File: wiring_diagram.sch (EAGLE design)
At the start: 9 parts, among them X1 22-23-2021, X2 22-23-2021, X3 22-23-2021, X4 22-23-2021, X5 22-23-2021, X6 22-23-2021, X7 22-23-2021, X8 22-23-2021, X9 22-23-2021

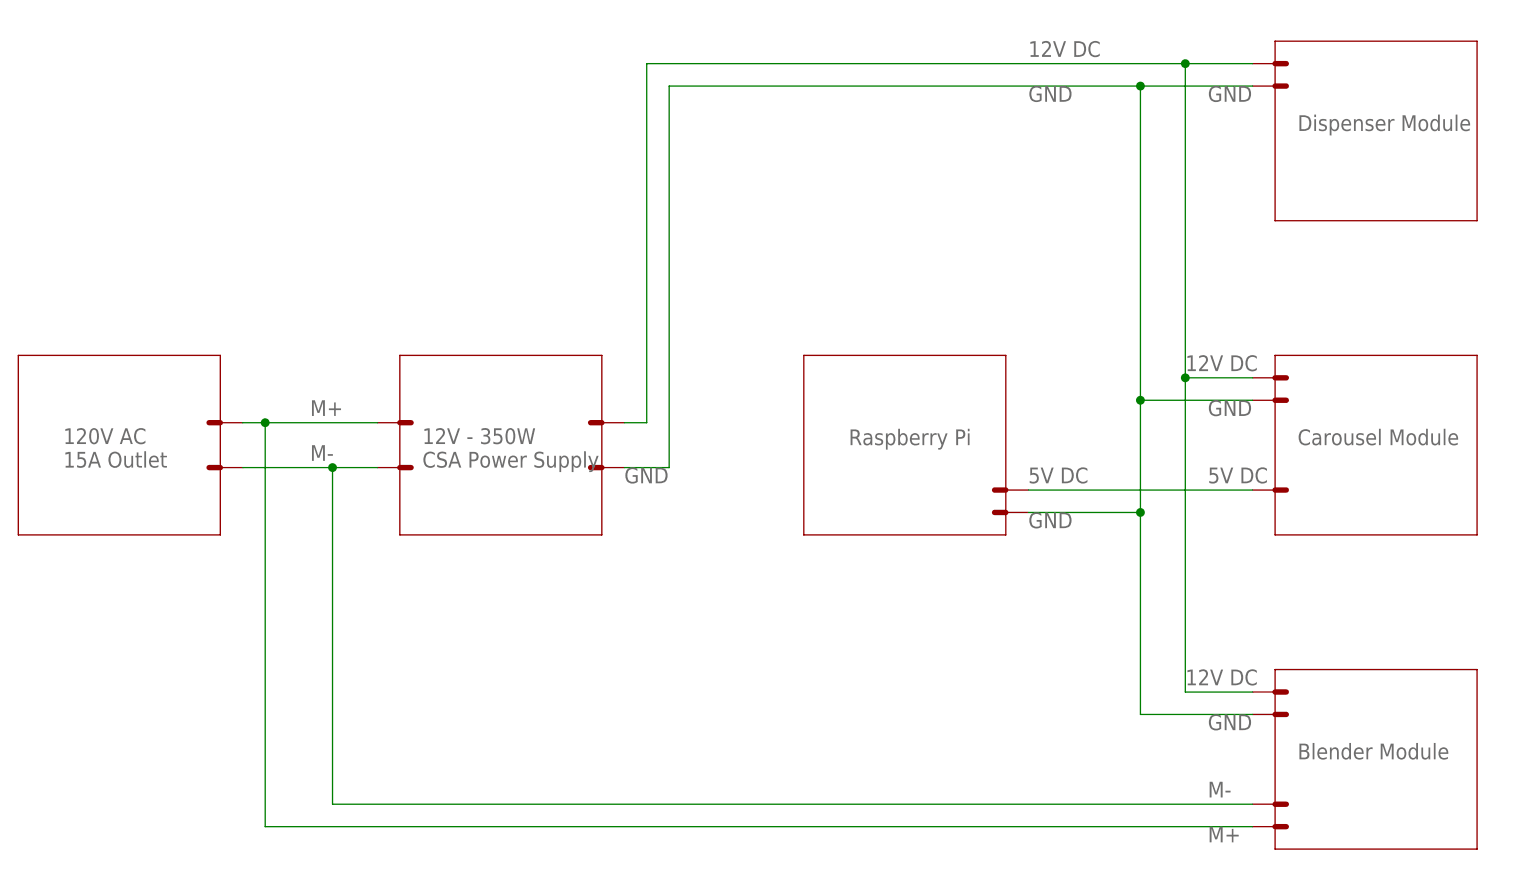
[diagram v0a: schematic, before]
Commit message: Added fuses and switch
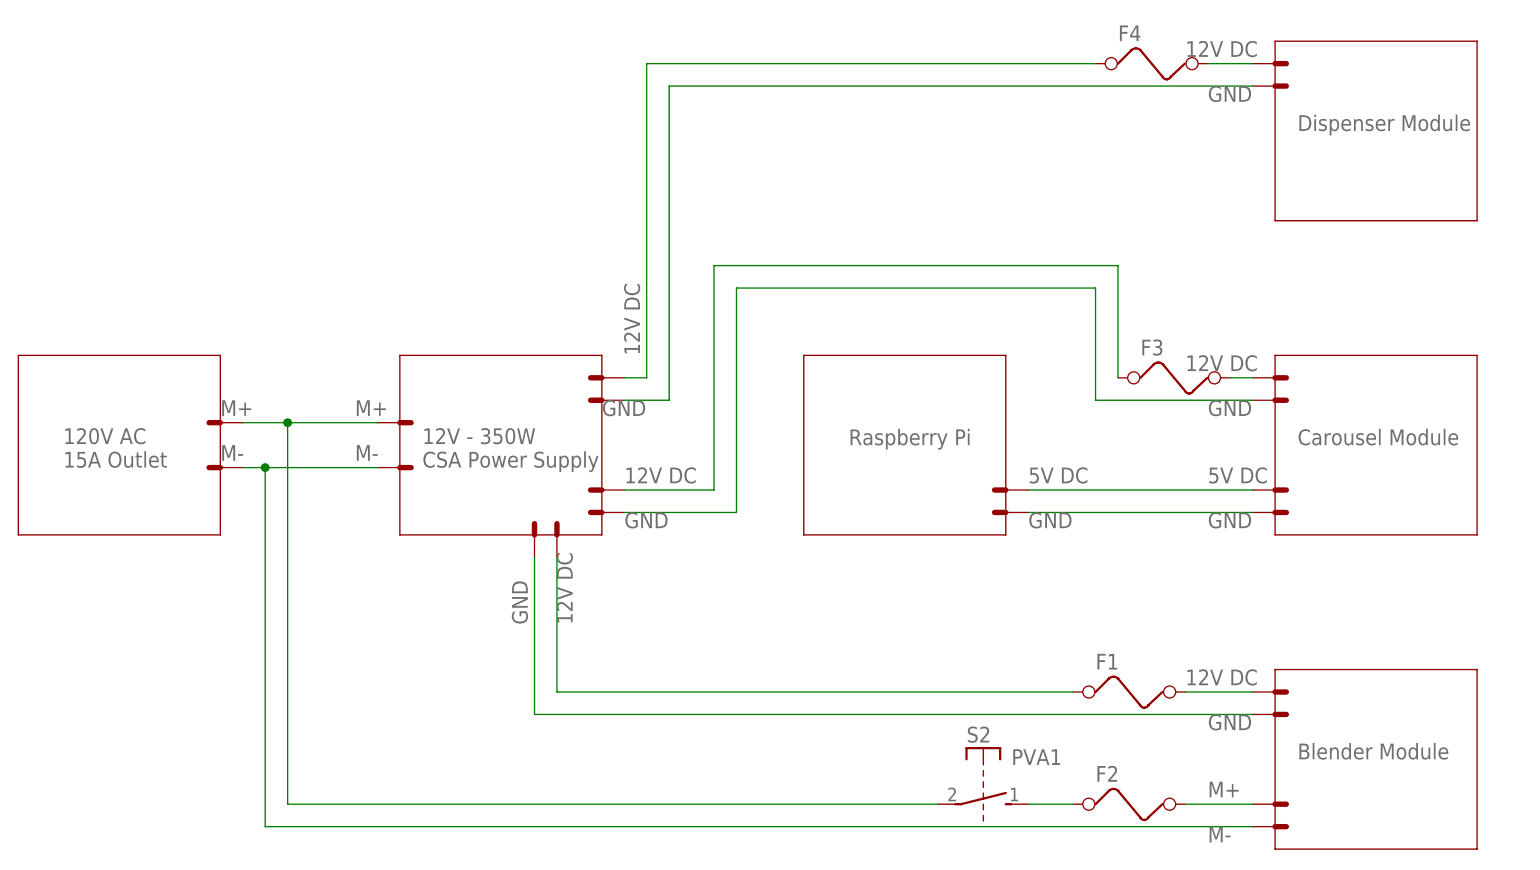
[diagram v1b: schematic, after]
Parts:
- added F1, F2, F3, F4: (no value), special:FUSE
- added S2: PVA1, switch-misc:PVA1
- added X10, X11, X12, X13, X14: 22-23-2021, con-molex:22-23-2021
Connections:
- new net N$10: X14-1.S, X7-2.S
- new net N$12: F1.2, X7-1.S
- new net N$13: F2.2, X8-1.S
- new net N$14: F3.2, X5-1.S
- new net N$15: F4.2, X6-1.S
- new net N$16: F2.1, S21.S
- new net N$17: X1-2.S, X2-1.S
- new net N$6: X10-1.S, X4-1.S
- new net N$7: F3.1, X12-1.S
- new net N$8: X11-1.S, X5-2.S
- new net N$9: F1.1, X13-1.S
- net N$1: now also X1-1.S, X2-2.S; no longer X1-2.S, X2-1.S
- net N$2: now also S21.P; no longer X1-1.S, X2-2.S, X8-1.S
- net N$3: now also F4.1; no longer X5-1.S, X6-1.S, X7-1.S
- net N$4: no longer X4-1.S, X5-2.S, X7-2.S
